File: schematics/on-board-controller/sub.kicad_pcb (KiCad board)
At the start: 2 copper layers, 90 x 60 mm, 75 parts, among them J1 5-1814832-1, J2 programmer, J3 xt60, M1 Motor_DC, M2 Motor_DC, M3 Stepper_Motor_bipolar, Q1 NMOS, U1 L293D, U2 STM32L476RGTx, U3 L293D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

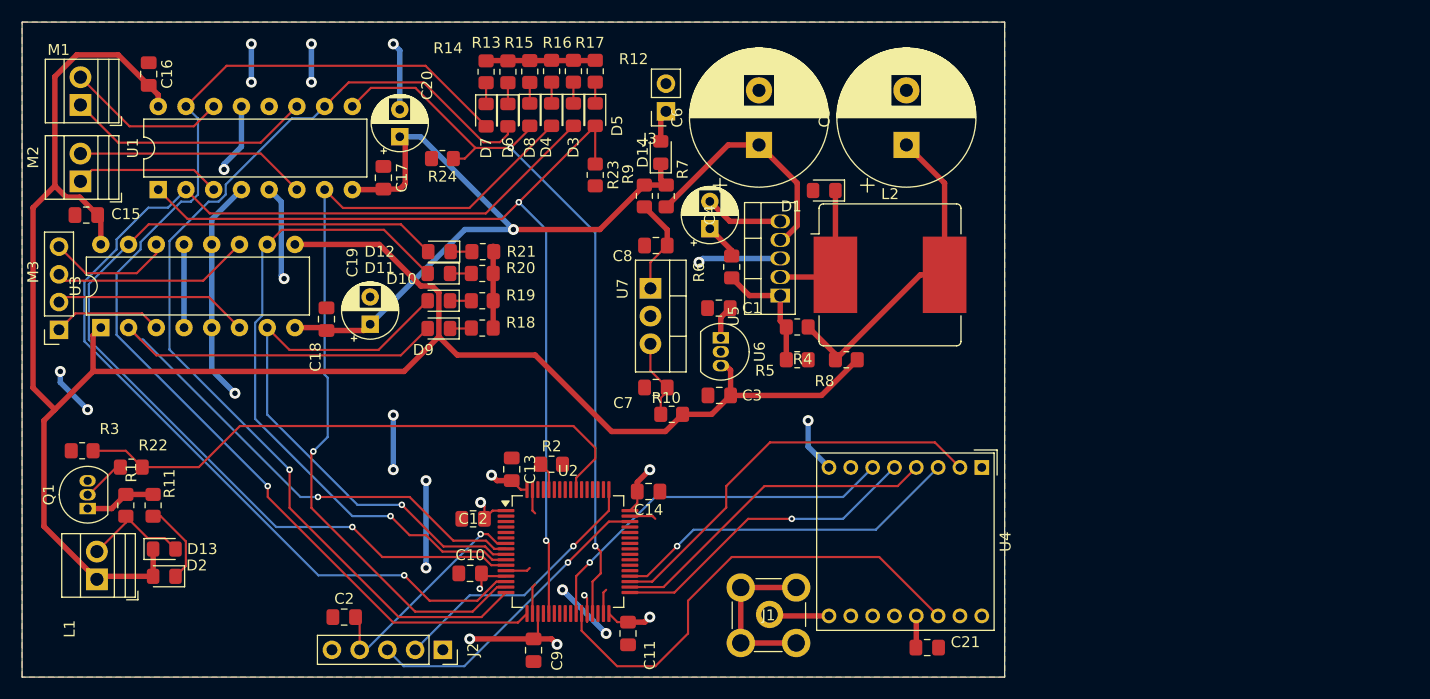
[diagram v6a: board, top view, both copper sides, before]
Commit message: updated silkscreen
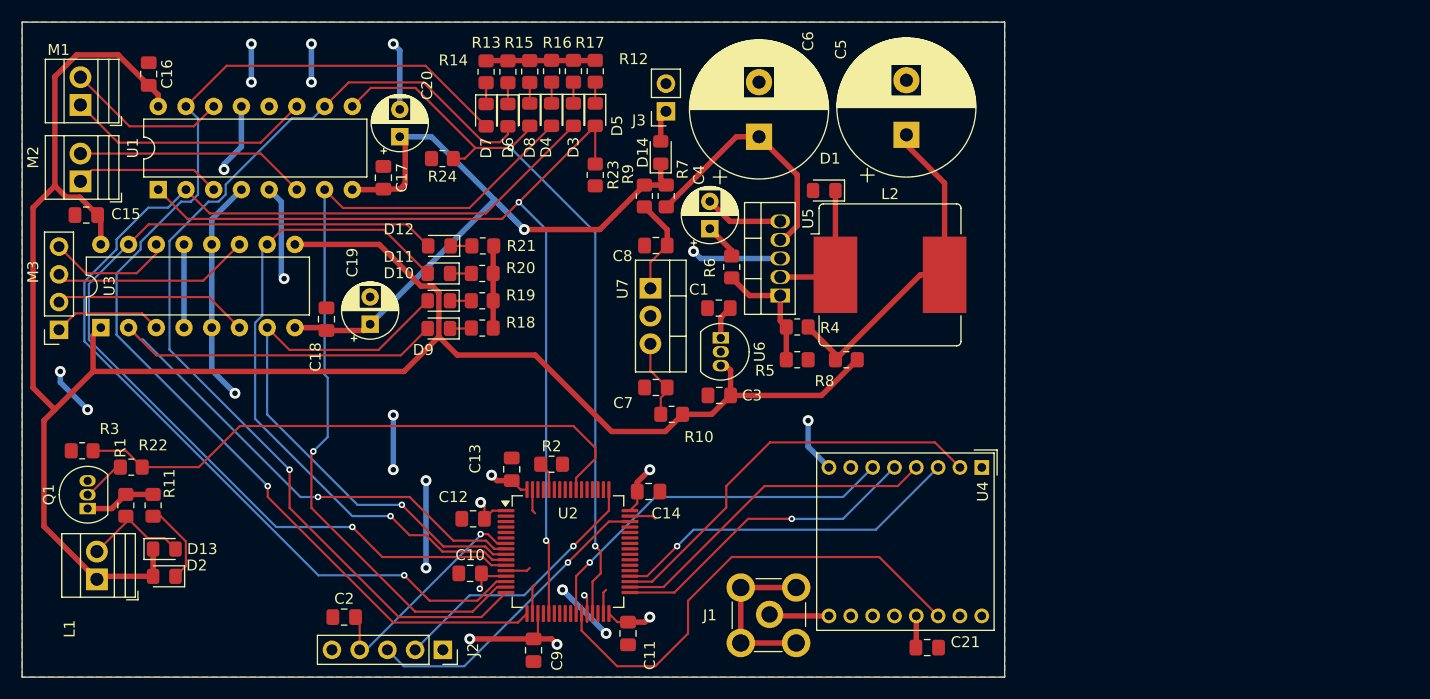
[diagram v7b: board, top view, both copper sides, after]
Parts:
- moved C5 0.93 mm to (143.5, 70.8)
- moved C6 0.75 mm to (130.0, 71.0)
- moved D12 0.53 mm to (100.7, 81.0)
- moved R21 0.53 mm to (104.7, 81.0)
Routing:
- net +BATT: track 65.3 -> 68.6 mm
- net Net-(U5-INPUT): track 21.8 -> 22.9 mm
- net Net-(C5-Pad1): track 31.1 -> 32.0 mm
- net GND: track 139.8 -> 140.5 mm
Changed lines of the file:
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@@
 		(tags "LED handsolder")
 		(property "Reference" "D11"
-			(at 5.425 0.5 0)
+			(at 3.675 1.525 0)
 			(layer "F.SilkS")
 			(effects
@@
 		(tags "capacitor handsolder")
 		(property "Reference" "C12"
-			(at 0 0 360)
+			(at -1.811029 -2 360)
 			(layer "F.SilkS")
 			(effects
@@
 		(at 130.8675 114.8325)
 		(property "Reference" "J1"
-			(at 0 0 0)
+			(at -5.3675 0 0)
 			(layer "F.SilkS")
 			(effects
@@
 		(tags "CP Radial series Radial pin pitch 2.50mm  diameter 5mm Electrolytic Capacitor")
 		(property "Reference" "C4"
-			(at 1.25 0 90)
+			(at 4.926041 -1 90)
 			(layer "F.SilkS")
 			(effects
@@
 		(tags "Through hole socket strip THT 1x02 2.54mm single row")
 		(property "Reference" "J3"
-			(at 1.475 -2.5 360)
+			(at 2.475 -0.823959 360)
 			(layer "F.SilkS")
 			(effects
@@
 		(tags "capacitor handsolder")
 		(property "Reference" "C1"
-			(at -3.0375 0 360)
+			(at 1.8225 1.696041 360)
 			(layer "F.SilkS")
 			(effects
@@
 		(tags "resistor handsolder")
 		(property "Reference" "R1"
-			(at 3 0.5 90)
+			(at 5.265 -0.5 90)
 			(layer "F.SilkS")
 			(effects
@@
 	(footprint "Resistor_SMD:R_0805_2012Metric_Pad1.20x1.40mm_HandSolder"
 		(layer "F.Cu")
-		(at 104.7 81.525)
+		(at 104.7 81)
 		(descr "Resistor SMD 0805 (2012 Metric), square (rectangular) end terminal, IPC_7351 nominal with elongated pad for handsoldering. (Body size source: IPC-SM-782 page 72, https://www.pcb-3d.com/wordpress/wp-content/uploads/ipc-sm-782a_amendment_1_and_2.pdf), generated with kicad-footprint-generator")
 		(tags "resistor handsolder")
@@
 		)
 		(fp_text user "${REFERENCE}"
-			(at 0 0 0)
+			(at 0 -0.025 0)
 			(layer "F.Fab")
 			(effects
@@
 		(tags "LED handsolder")
 		(property "Reference" "D10"
-			(at 3.425 2 0)
+			(at 3.675 2.525 0)
 			(layer "F.SilkS")
 			(effects
@@
 		(tags "TO-220-5 Vertical RM 1.7mm Pentawatt Multiwatt-5")
 		(property "Reference" "U5"
-			(at -1.87623 -4.27 90)
+			(at 7.049811 2.555 90)
 			(layer "F.SilkS")
 			(effects
@@
 	(footprint "Capacitor_THT:CP_Radial_D12.5mm_P5.00mm"
 		(layer "F.Cu")
-		(at 130 71.75 90)
+		(at 130 71 90)
 		(descr "CP, Radial series, Radial, pin pitch=5.00mm, , diameter=12.5mm, Electrolytic Capacitor")
 		(tags "CP Radial series Radial pin pitch 5.00mm  diameter 12.5mm Electrolytic Capacitor")
 		(property "Reference" "C6"
-			(at 2.5 -7.5 90)
+			(at 8.75 4.5 90)
 			(layer "F.SilkS")
 			(effects
@@
 		(tags "capacitor handsolder")
 		(property "Reference" "C13"
-			(at 0 -1.68 90)
+			(at -0.9625 3.348529 90)
 			(layer "F.SilkS")
 			(effects
@@
 		(tags "Low Power Long Range Transceiver Module LoRa")
 		(property "Reference" "U4"
-			(at 6.8 -2.17 90)
+			(at 2.2075 -0.0925 90)
 			(layer "F.SilkS")
 			(effects
@@
 		(tags "LQFP QFP")
 		(property "Reference" "U2"
-			(at 0 -7.4 360)
+			(at 0 -3.5 360)
 			(layer "F.SilkS")
 			(effects
@@
 		(tags "resistor handsolder")
 		(property "Reference" "R14"
-			(at 2.165 -3.49 180)
+			(at 1.05 -3 180)
 			(layer "F.SilkS")
 			(effects
@@
 		(tags "THT DIP DIL PDIP 2.54mm 7.62mm 300mil")
 		(property "Reference" "U3"
-			(at 3.81 -2.33 90)
+			(at 3.81 0.79 90)
 			(layer "F.SilkS")
 			(effects
@@
 		(tags "diode handsolder")
 		(property "Reference" "D1"
-			(at 3.025 -1.452271 360)
+			(at -0.525 2.926041 360)
 			(layer "F.SilkS")
 			(effects
@@
 	(footprint "Capacitor_THT:CP_Radial_D12.5mm_P5.00mm"
 		(layer "F.Cu")
-		(at 143.5 71.75 90)
+		(at 143.5 70.823959 90)
 		(descr "CP, Radial series, Radial, pin pitch=5.00mm, , diameter=12.5mm, Electrolytic Capacitor")
 		(tags "CP Radial series Radial pin pitch 5.00mm  diameter 12.5mm Electrolytic Capacitor")
 		(property "Reference" "C5"
-			(at 2.5 -7.5 90)
+			(at 7.823959 -6 90)
 			(layer "F.SilkS")
 			(effects
@@
 	(footprint "LED_SMD:LED_0805_2012Metric_Pad1.15x1.40mm_HandSolder"
 		(layer "F.Cu")
-		(at 100.725 81.525 180)
+		(at 100.725 81 180)
 		(descr "LED SMD 0805 (2012 Metric), square (rectangular) end terminal, IPC_7351 nominal, (Body size source: https://docs.google.com/spreadsheets/d/1BsfQQcO9C6DZCsRaXUlFlo91Tg2WpOkGARC1WS5S8t0/edit?usp=sharing), generated with kicad-footprint-generator")
 		(tags "LED handsolder")
 		(property "Reference" "D12"
-			(at 5.475 0 0)
+			(at 3.725 1.525 0)
 			(layer "F.SilkS")
 			(effects
@@
 		(tags "resistor handsolder")
 		(property "Reference" "R10"
-			(at 0.5 1.5 360)
+			(at -2.5 -2.073959 360)
 			(layer "F.SilkS")
 			(effects
@@
 		(tags "resistor handsolder")
 		(property "Reference" "R4"
-			(at 0.5 2.952271 360)
+			(at 3 0.073959 360)
 			(layer "F.SilkS")
 			(effects
@@
 		(tags "resistor handsolder")
 		(property "Reference" "R6"
-			(at 0.5 3 90)
+			(at 0.073959 2 90)
 			(layer "F.SilkS")
 			(effects
@@
 		(tags "capacitor handsolder")
 		(property "Reference" "C14"
-			(at 0 -1.68 360)
+			(at -1.613971 -2 360)
 			(layer "F.SilkS")
 			(effects
@@
 	)
 	(via
-		(at 124.5 82.5)
+		(at 124 81.5)
 		(size 1)
 		(drill 0.5)
@@
 	)
 	(segment
+		(start 124 81.5)
+		(end 124.649811 82.149811)
+		(width 0.5)
+		(layer "B.Cu")
+		(net 2)
+	)
+	(segment
 		(start 79.87 88.485)
 		(end 79.87 80.865)
@@
 	)
 	(segment
+		(start 124.649811 82.149811)
+		(end 131.945 82.149811)
+		(width 0.5)
+		(layer "B.Cu")
+		(net 2)
+	)
+	(segment
 		(start 82.59 71.91)
 		(end 82.59 68.225)
@@
 	)
 	(segment
-		(start 124.5 82.5)
-		(end 124.850189 82.149811)
-		(width 0.5)
-		(layer "B.Cu")
-		(net 2)
-	)
-	(segment
-		(start 124.850189 82.149811)
-		(end 131.945 82.149811)
-		(width 0.5)
-		(layer "B.Cu")
-		(net 2)
-	)
-	(segment
 		(start 97.095 68.500113)
 		(end 97.095 63.095)
@@
 	)
 	(segment
-		(start 131.1025 114.8925)
-		(end 130.9675 114.7575)
-		(width 0.5)
-		(layer "F.Cu")
-		(net 3)
-	)
-	(segment
 		(start 118 115.4625)
 		(end 117.0375 115.4625)
@@
 	)
 	(segment
-		(start 115.426041 79.5)
-		(end 107.5 79.5)
-		(width 0.5)
-		(layer "F.Cu")
-		(net 20)
-	)
-	(segment
 		(start 95.545 75.845)
 		(end 95.595 75.795)
@@
 	)
 	(segment
-		(start 119.5 75.426041)
-		(end 115.426041 79.5)
+		(start 115.426041 79.5)
+		(end 119.5 75.426041)
 		(width 0.5)
 		(layer "F.Cu")
@@
 	)
 	(segment
+		(start 108.5 79.5)
+		(end 115.426041 79.5)
+		(width 0.5)
+		(layer "F.Cu")
+		(net 20)
+	)
+	(segment
 		(start 97.095 75.795)
 		(end 97.595 75.295)
@@
 	)
 	(via
-		(at 107.5 79.5)
+		(at 108.5 79.5)
 		(size 1)
 		(drill 0.5)
@@
 	)
 	(segment
-		(start 107.5 79.5)
-		(end 99.000113 71.000113)
+		(start 108.5 79.5)
+		(end 100.000113 71.000113)
 		(width 0.5)
 		(layer "B.Cu")
@@
 	)
 	(segment
-		(start 99.000113 71.000113)
-		(end 97.095 71.000113)
+		(start 105.777328 76.777329)
+		(end 94.38 88.174657)
 		(width 0.5)
 		(layer "B.Cu")
@@
 	)
 	(segment
-		(start 107.5 79.5)
-		(end 103.054657 79.5)
+		(start 100.000113 71.000113)
+		(end 97.095 71.000113)
 		(width 0.5)
 		(layer "B.Cu")
@@
 	)
 	(segment
-		(start 103.054657 79.5)
-		(end 94.38 88.174657)
+		(start 108.5 79.5)
+		(end 105.777328 76.777329)
 		(width 0.5)
 		(layer "B.Cu")
@@
 	)
 	(segment
-		(start 74.09 79.025)
-		(end 72.25 80.865)
+		(start 99.7 81)
+		(end 97.725 79.025)
 		(width 0.2)
 		(layer "F.Cu")
@@
 	)
 	(segment
-		(start 92.75 106.75)
-		(end 95.5 109.5)
+		(start 74.09 79.025)
+		(end 72.25 80.865)
 		(width 0.2)
 		(layer "F.Cu")
@@
 	)
 	(segment
-		(start 99.7 81.525)
-		(end 97.2 79.025)
+		(start 92.75 106.75)
+		(end 95.5 109.5)
 		(width 0.2)
 		(layer "F.Cu")
@@
 	)
 	(segment
-		(start 97.2 79.025)
-		(end 74.09 79.025)
+		(start 105.472887 110.25)
+		(end 106.825 110.25)
 		(width 0.2)
 		(layer "F.Cu")
@@
 	)
 	(segment
-		(start 105.472887 110.25)
-		(end 106.825 110.25)
+		(start 97.725 79.025)
+		(end 74.09 79.025)
 		(width 0.2)
 		(layer "F.Cu")
@@
 	)
 	(segment
-		(start 147 75.25)
-		(end 143.5 71.75)
+		(start 143.5 71.75)
+		(end 143.5 70.823959)
 		(width 0.5)
 		(layer "F.Cu")
@@
 	)
 	(segment
+		(start 147 75.25)
+		(end 143.5 71.75)
+		(width 0.5)
+		(layer "F.Cu")
+		(net 74)
+	)
+	(segment
 		(start 147 83.649811)
 		(end 144.77623 83.649811)
@@
 	)
 	(segment
-		(start 133.5 79.157311)
-		(end 133.5 75.25)
+		(start 127.926041 71)
+		(end 130 71)
 		(width 0.5)
 		(layer "F.Cu")
@@
 	)
 	(segment
-		(start 127.176041 71.75)
-		(end 130 71.75)
+		(start 130 71)
+		(end 133.5 74.5)
 		(width 0.5)
 		(layer "F.Cu")
@@
 	)
 	(segment
-		(start 133.5 75.25)
-		(end 130 71.75)
+		(start 121.5 77.426041)
+		(end 127.926041 71)
 		(width 0.5)
 		(layer "F.Cu")
@@
 	)
 	(segment
-		(start 131.945 80.449811)
+		(start 133.5 79.157311)
 		(end 132.2075 80.449811)
 		(width 0.5)
@@
 	)
 	(segment
-		(start 132.2075 80.449811)
+		(start 133.5 74.5)
 		(end 133.5 79.157311)
 		(width 0.5)
@@
 	)
 	(segment
-		(start 121.5 77.426041)
-		(end 127.176041 71.75)
+		(start 132.2075 80.449811)
+		(end 131.945 80.449811)
 		(width 0.5)
 		(layer "F.Cu")
@@
 	)
 	(segment
-		(start 101.75 81.525)
-		(end 103.7 81.525)
+		(start 101.75 81)
+		(end 103.7 81)
 		(width 0.2)
 		(layer "F.Cu")
